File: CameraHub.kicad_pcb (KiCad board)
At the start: 4 copper layers, 90.2 x 95.9 mm, 121 parts, among them J1 200528-0100, J10 TE_282834-4, J2 Header 01x04 0.1", J3 Header 01x04 0.1", J4 USB_C_Receptacle_USB2.0_16P, J5 USB_C_Receptacle_USB2.0_16P, J6 Header 01x04 0.1", J7 USB_C_Receptacle_USB2.0_16P, J8 USB_C_Receptacle_USB2.0_16P, J9 Header 01x04 0.1"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

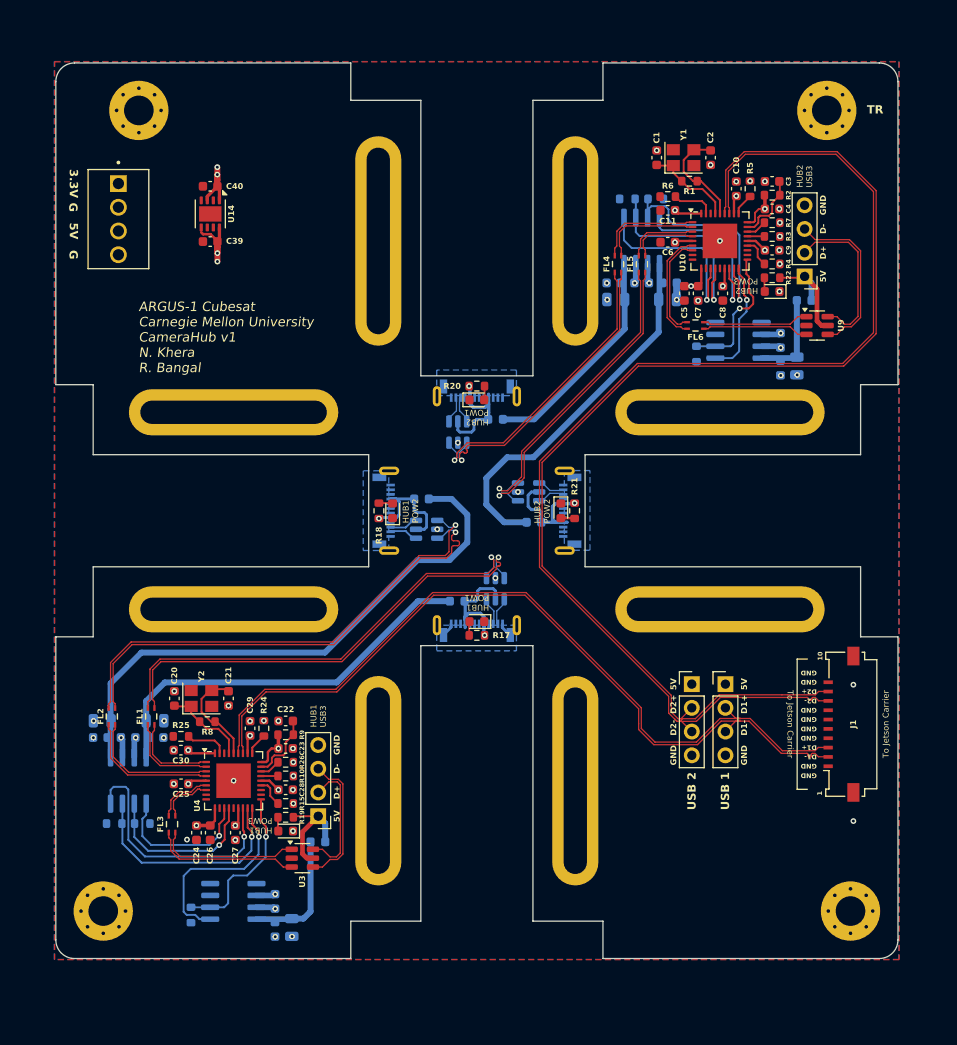
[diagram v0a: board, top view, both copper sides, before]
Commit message: Finished Camera Hub
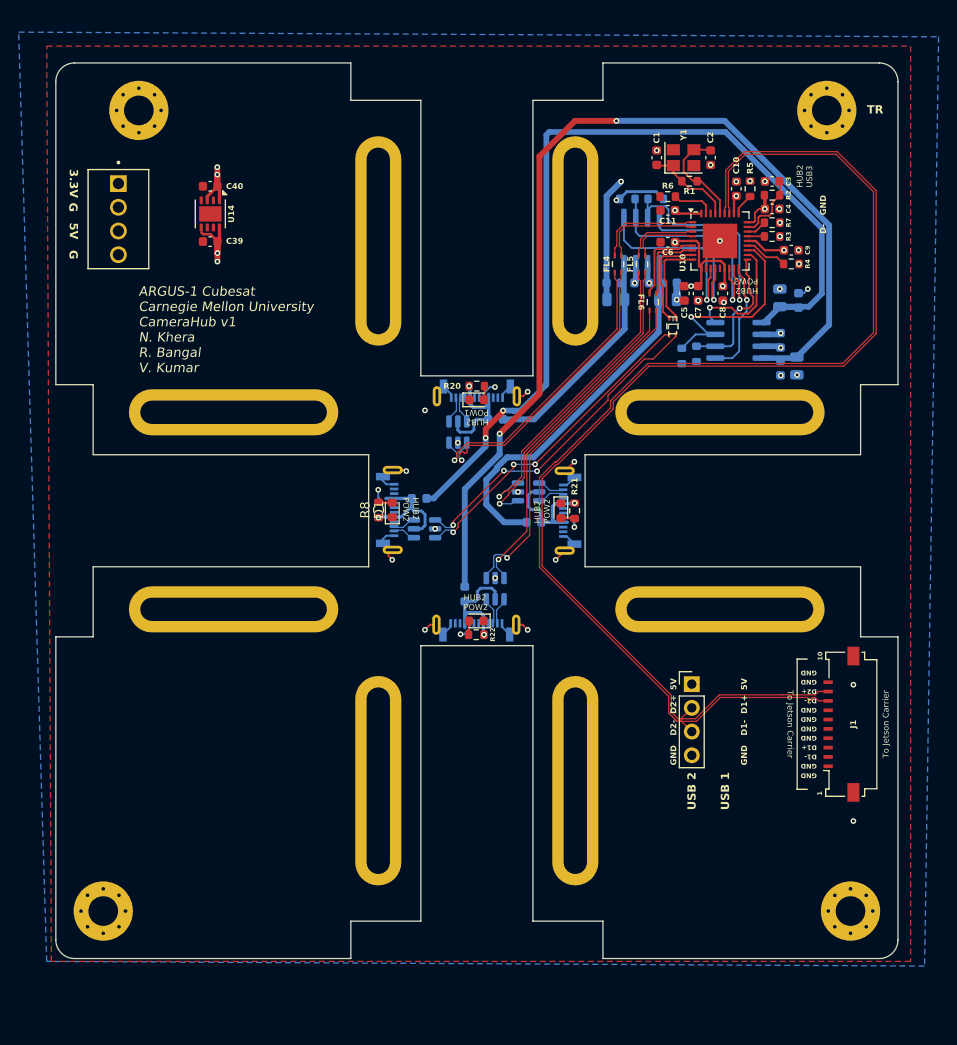
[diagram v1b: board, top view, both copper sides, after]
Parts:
- removed C22, C25, C26, C27, C28, C29, C30, C31, C33, C35, C36, C38: 0.1uF, Capacitor_SMD:C_0603_1608Metric
- removed C23: 4.7uF, Capacitor_SMD:C_0603_1608Metric
- removed C24: 1uF, Capacitor_SMD:C_0603_1608Metric
- removed C32, C34, C37: 100uF, Capacitor_SMD:C_0805_2012Metric
- removed D2, D3: Green, LED_SMD:LED_0603_1608Metric
- removed FB4, FB6: 600R, Inductor_SMD:L_0603_1608Metric
- removed FL2, FL3: 744230900, CameraHub:CHIP_230900_WRE
- removed J5: USB_C_Receptacle_USB2.0_16P, CameraHub:USBC-121SMT-4BS2S
- removed J6, J9: Header 01x04 0.1", Connector_PinHeader_2.54mm:PinHeader_1x04_P2.54mm_Vertical
- removed R10, R15, R24, R26: 36K, Resistor_SMD:R_0603_1608Metric
- removed R17, R18, R19: 330R, Resistor_SMD:R_0603_1608Metric
- removed R25: 12K, Resistor_SMD:R_0603_1608Metric
- removed R30, R31, R33: 10K, Resistor_SMD:R_0603_1608Metric
- removed U2, U3: USBLC6-2P6, Package_TO_SOT_SMD:SOT-23-6
- removed U4: USB2514B-I/M2, Package_DFN_QFN:QFN-36-1EP_6x6mm_P0.5mm_EP3.7x3.7mm
- removed U5, U6: MIC2026-1xM, Package_SO:SOIC-8_3.9x4.9mm_P1.27mm
- removed Y2: 24MHz, Crystal:Crystal_SMD_3225-4Pin_3.2x2.5mm
- C20: value 27pF -> 100uF; footprint Capacitor_SMD:C_0603_1608Metric -> Capacitor_SMD:C_0805_2012Metric; moved to B.Cu
- C21: value 27pF -> 0.1uF; moved to B.Cu
- J2: value Header 01x04 0.1" -> USB_C_Receptacle_USB2.0_16P; footprint Connector_PinHeader_2.54mm:PinHeader_1x04_P2.54mm_Vertical -> CameraHub:USBC-121SMT-4BS2S; moved to B.Cu
- R8: value 1M -> 330R
- R9: value 100K -> 10K; moved to B.Cu
- U9: moved to B.Cu
- moved C20 77.7 mm to (181.3, 74.0)
- moved C21 74.4 mm to (183.3, 74.3), turned to 90 degrees
- moved FL1 69.7 mm to (169.8, 77.1), turned to -90 degrees
- moved R9 58.7 mm to (170.8, 80.3), turned to 90 degrees
- moved R22 49.6 mm to (148.8, 110.1)
- moved D6 47.4 mm to (148.8, 108.6)
- moved U9 44.5 mm to (150.9, 105.2), turned to -90 degrees
- moved FB3 38.3 mm to (142.7, 95.5), turned to 180 degrees
- moved R8 29.2 mm to (138.4, 96.7), turned to 90 degrees
- moved J2 27.5 mm to (148.8, 108.9), turned to 180 degrees
- moved J4 15.1 mm to (140.0, 96.7), turned to 90 degrees
- moved D1 15.0 mm to (139.8, 96.7), turned to 90 degrees
- moved U1 9.94 mm to (143.3, 98.8), turned to 180 degrees
- moved FL6 5.21 mm to (167.7, 74.5), turned to -90 degrees
- moved C9 2.05 mm to (182.6, 68.9)
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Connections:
- net /Hub 1/D1_N renamed /Hub 2/D4_N
- net /Hub 1/D1_P renamed /Hub 2/D4_P
- net /Hub 1/FD1_N renamed /Hub 2/FD4_N
- net /Hub 1/FD1_P renamed /Hub 2/FD4_P
- C20 pad 1: Net-(U4-XTALIN/CLKIN) -> /Hub 2/VBUS4
- C21 pad 1: Net-(U4-XTALOUT) -> /Hub 2/VBUS4
- FB1 pad 1: /Hub 1/VBUS1 -> /Hub 2/VBUS3
- FB1 pad 2: /Hub 1/VBUS_CONN1 -> /Hub 2/VBUS_CONN3
- FB3 pad 1: /Hub 1/VBUS3 -> /Hub 2/VBUS4
- FB3 pad 2: /Hub 1/VBUS_CONN3 -> /Hub 2/VBUS_CONN4
- FL1 pad 1: /Hub 1/HD1_P -> /Hub 2/HD4_P
- FL1 pad 4: /Hub 1/HD1_N -> /Hub 2/HD4_N
- J1 pad 2: /USB1_N -> unconnected-(J1-Pin_2-Pad2)
- J1 pad 3: /USB1_P -> unconnected-(J1-Pin_3-Pad3)
- J4 pad A4: /Hub 1/VBUS_CONN1 -> /Hub 2/VBUS_CONN4
- J4 pad B9: /Hub 1/VBUS_CONN1 -> /Hub 2/VBUS_CONN4
- R8 pad 1: Net-(U4-XTALIN/CLKIN) -> /Hub 2/VBUS_CONN4
- R8 pad 2: Net-(U4-XTALOUT) -> Net-(D1-A)
- R9 pad 1: /nRST1 -> +3.3V
- R9 pad 2: +3.3V -> /Hub 2/nOCS4
- U1 pad 5: /Hub 1/VBUS_CONN1 -> /Hub 2/VBUS_CONN4
- U10 pad 20: unconnected-(U10-PRTPWR4/BC_EN4-Pad20) -> /Hub 2/PWR4
- U10 pad 21: unconnected-(U10-OCS_N4-Pad21) -> /Hub 2/nOCS4
- U10 pad 8: unconnected-(U10-USBDM_DN4/PRT_DIS_M4-Pad8) -> /Hub 2/HD4_N
- U10 pad 9: unconnected-(U10-USBDP_DN4/PRT_DIS_P4-Pad9) -> /Hub 2/HD4_P
- U12 pad 3: unconnected-(U12-FLGB-Pad3) -> /Hub 2/nOCS4
- U12 pad 4: unconnected-(U12-ENB-Pad4) -> /Hub 2/PWR4
- U12 pad 5: unconnected-(U12-OUTB-Pad5) -> /Hub 2/VBUS4
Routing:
- net /Hub 2/VBUS4: track 0.00 -> 96.5 mm, vias 0 -> 2
- net /Hub 2/VBUS3: track 9.88 -> 106.0 mm, vias 0 -> 2
- net /USB1_P: track 85.8 -> 0.00 mm
- net /USB1_N: track 85.6 -> 0.00 mm
- net /Hub 1/VBUS2: track 60.2 -> 0.00 mm
- net /Hub 1/FD2_N: track 52.0 -> 0.00 mm, vias 1 -> 0
- net /Hub 1/FD2_P: track 51.6 -> 0.00 mm, vias 1 -> 0
- net /Hub 1/VBUS1: track 42.2 -> 0.00 mm
- net GND: track 13.4 -> 51.3 mm, vias 50 -> 39
- net /Hub 1/PWR2: track 26.8 -> 0.00 mm, vias 1 -> 0
- net /Hub 2/FD3_P: track 11.4 -> 37.4 mm, vias 0 -> 1
- net /Hub 2/FD3_N: track 11.4 -> 35.8 mm, vias 0 -> 1
- net /Hub 1/nOCS2: track 24.2 -> 0.00 mm, vias 1 -> 0
- net /Hub 2/nOCS4: track 0.00 -> 23.0 mm, vias 0 -> 1
- net /Hub 1/PWR3: track 21.2 -> 0.00 mm, vias 1 -> 0
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- removed copper zone on B.Cu, net GND
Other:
- board text added: "ARGUS-1 Cubesat Carnegie Mellon University CameraHub v1 N. Khera R. Bangal V. Kumar"
- board text removed: "ARGUS-1 Cubesat Carnegie Mellon University CameraHub v1 N. Khera R. Bangal"
- board text removed: "D+"
- board text removed: "HUB1 POW1"
- board text removed: "HUB1 POW2"
- board text removed: "HUB1 POW3"
- board text removed: "HUB1 USB3"

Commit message: rev2.1
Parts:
- removed J1: 200528-0100, Connector_FFC-FPC:Molex_200528-0100_1x10-1MP_P1.00mm_Horizontal
- removed J10: TE_282834-4, CameraHub:TE_282834-4
- added C22: 1uF, Capacitor_SMD:C_0603_1608Metric, F.Cu at (185.3, 123.6)
- added J5: 200528-0100, Connector_FFC-FPC:Molex_200528-0100_1x10-1MP_P1.00mm_Horizontal, B.Cu at (189.5, 123.1)
- moved C40 89.9 mm to (179.8, 129.4)
- moved C39 89.9 mm to (179.8, 135.3)
- moved U14 89.9 mm to (179.9, 132.4)
- moved R8 20.8 mm to (159.2, 96.9), turned to -90 degrees
- moved R21 20.7 mm to (138.6, 96.8), turned to 90 degrees
- moved J8 18.3 mm to (139.8, 96.8), turned to 90 degrees
- moved J4 17.9 mm to (158.0, 96.8), turned to -90 degrees
- moved D1 17.9 mm to (157.7, 96.9), turned to -90 degrees
- moved D5 17.8 mm to (140.1, 96.8), turned to 90 degrees
- moved FB5 12.3 mm to (143.0, 95.6), turned to 180 degrees
- moved FB3 12.2 mm to (154.7, 98.1), turned to 0 degrees
- moved U8 11.6 mm to (143.6, 98.8), turned to 180 degrees
- moved U1 11.5 mm to (154.1, 94.8), turned to 0 degrees
- moved C1 6.41 mm to (174.6, 59.0)
- moved C10 6.41 mm to (183.1, 62.4)
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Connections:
- net /USB2_N renamed /USB_N
- net /USB2_P renamed /USB_P
- net /nRST2 renamed /nRST
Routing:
- net /Hub 2/VBUS4: track 96.5 -> 76.2 mm, vias 2 -> 4
- net /Hub 2/VBUS2: track 40.2 -> 53.3 mm, vias 0 -> 2
- net +5V: track 10.8 -> 22.8 mm, vias 4 -> 9
- net /Hub 2/PWR3: track 12.4 -> 20.7 mm
- net /Hub 2/HD2_N: track 7.76 -> 16.0 mm
- net /Hub 2/HD2_P: track 7.30 -> 15.5 mm
- net /Hub 2/HD1_P: track 10.7 -> 18.0 mm
- net /Hub 2/HD1_N: track 11.2 -> 18.5 mm
- net /Hub 2/nOCS3: track 14.9 -> 20.5 mm
- net /Hub 2/FD2_P: track 33.3 -> 38.9 mm
- net /Hub 2/FD2_N: track 33.1 -> 38.6 mm
- net /Hub 2/VBUS3: track 106.0 -> 100.5 mm, vias 2 -> 4
- net /Hub 2/PWR4: track 13.5 -> 18.5 mm
- net /Hub 2/FD4_P: track 35.4 -> 30.7 mm, vias 3 -> 1
- net /Hub 2/FD4_N: track 34.8 -> 30.8 mm, vias 3 -> 1
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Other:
- board text added: "HUB1 USB3"
- board text added: "HUB1 USB4"
- board text removed: "10"
- board text removed: "3.3V"
- board text removed: "G"
- board text removed: "HUB2 USB1"
- board text removed: "HUB2 USB2"

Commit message: Add files via upload
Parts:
- moved C21 7.34 mm to (183.8, 78.6), turned to 0 degrees
- moved C20 4.70 mm to (184.0, 76.9), turned to 0 degrees
- moved C18 0.22 mm to (183.2, 81.5)
- moved C19 0.17 mm to (181.4, 81.7)
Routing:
- net /Hub 2/VBUS3: track 100.5 -> 51.3 mm, vias 4 -> 0
- net /Hub 2/PWR3: track 20.7 -> 11.6 mm
- net /Hub 2/VBUS4: track 76.2 -> 67.7 mm, vias 4 -> 2
- net /Hub 2/VBUS2: track 53.3 -> 46.6 mm, vias 2 -> 0
- net /Hub 2/nOCS3: track 20.5 -> 16.3 mm
- net GND: track 54.0 -> 50.6 mm, vias 45 -> 41
- net +5V: track 22.8 -> 20.2 mm, vias 9 -> 8
- net /Hub 2/FD1_P: track 29.1 -> 31.3 mm
- net /Hub 2/FD1_N: track 28.9 -> 31.2 mm
- net /Hub 2/FD2_P: track 38.9 -> 37.8 mm
- net /Hub 2/VBUS1: track 23.9 -> 23.0 mm
- net /Hub 2/FD2_N: track 38.6 -> 37.9 mm

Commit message: rev2?'
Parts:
- moved C20 13.3 mm to (171.9, 82.4), turned to 180 degrees
- moved R9 12.8 mm to (183.5, 82.3)
- moved C21 11.9 mm to (172.1, 80.7), turned to 180 degrees
- moved R16 11.1 mm to (183.5, 79.3), turned to -90 degrees
- moved C18 11.1 mm to (172.8, 77.8), turned to 90 degrees
- moved C19 8.01 mm to (174.5, 77.6), turned to 90 degrees
- moved C17 7.22 mm to (174.5, 80.7), turned to -90 degrees
- moved U12 3.01 mm to (179.0, 80.7), turned to 180 degrees
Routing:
- net /Hub 2/VBUS4: track 67.7 -> 42.1 mm, vias 2 -> 0
- net GND: track 50.6 -> 39.7 mm, vias 41 -> 35
- net /USB_P: track 134.7 -> 142.8 mm
- net /Hub 2/FD3_N: track 37.7 -> 45.6 mm
- net /USB_N: track 134.8 -> 142.7 mm
- net /Hub 2/FD3_P: track 38.0 -> 44.7 mm
- net /Hub 2/VBUS3: track 51.3 -> 45.6 mm
- net /Hub 2/nOCS4: track 24.2 -> 20.7 mm, vias 1 -> 2
- net /Hub 2/nOCS3: track 16.3 -> 13.8 mm
- net /Hub 2/PWR3: track 11.6 -> 9.45 mm
- net /Hub 2/PWR4: track 18.5 -> 16.7 mm
- net /Hub 2/FD4_P: track 30.7 -> 31.8 mm
- net /Hub 2/FD4_N: track 30.8 -> 31.7 mm
